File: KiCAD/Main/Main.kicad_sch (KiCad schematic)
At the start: 6 parts, among them J3 Conn_01x02_Socket, J6 Conn_01x02_Socket, J7 Conn_01x02_Socket, J8 Conn_01x02_Socket, U5 LT3092xST, U6 ADG5234BRUZ

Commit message: Add new rf
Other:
- added sheet RF (RF/RF.kicad_sch)
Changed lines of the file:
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@@
+	)
+	(sheet
+		(at 19.05 17.78)
+		(size 27.94 27.94)
+		(exclude_from_sim no)
+		(in_bom yes)
+		(on_board yes)
+		(dnp no)
+		(fields_autoplaced yes)
+		(stroke
+			(width 0.1524)
+			(type solid)
+		)
+		(fill
+			(color 0 0 0 0.0000)
+		)
+		(property "Sheetname" "RF"
+			(at 19.05 17.0684 0)
+			(effects
+				(font
+					(size 1.27 1.27)
+				)
+				(justify left bottom)
+			)
+		)
+		(property "Sheetfile" "RF/RF.kicad_sch"
+			(at 19.05 46.3046 0)
+			(effects
+				(font
+					(size 1.27 1.27)
+				)
+				(justify left top)
+			)
+		)
+		(instances
+			(project "Main"
+				(path "/bbb10697-a5dd-43b8-9c6f-4c5919cf3463"
+					(page "7")
+				)
+			)
+		)
 	)
 	(sheet

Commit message: post meeting update
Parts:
- removed J3, J6, J7, J8: Conn_01x02_Socket, symbol Connector:Conn_01x02_Socket
- removed U5: LT3092xST, Package_TO_SOT_SMD:SOT-223-3_TabPin2, symbol Reference_Current:LT3092xST
- removed U6: ADG5234BRUZ, ADG5234BRUZ:SOP65P640X120-20N, symbol ADG5234BRUZ:ADG5234BRUZ
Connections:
- no-connect marks 4 -> 0
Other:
- sheet GPS & Radio renamed GPS
- added sheet Barometer (Barometric Altimeter/Barometric Altimeter.kicad_sch)
- added sheet Thermistors (Thermistors/Thermistors.kicad_sch)
- sheet GPS ports: added GPS_SCL, GPS_SDA; removed GPS_UART_RX, GPS_UART_TX
- sheet Microcontroller ports: added GPS SCL, GPS SDA, Thermistor_SW1, Thermistor_SW2, Thermistor_SW3, Thermistor_SW4; removed GPS_RX, GPS_TX
- sheet RF ports: added CS_Radio, MISO_Radio, MOSI_Radio, RST_Radio, SCK_Radio; removed none

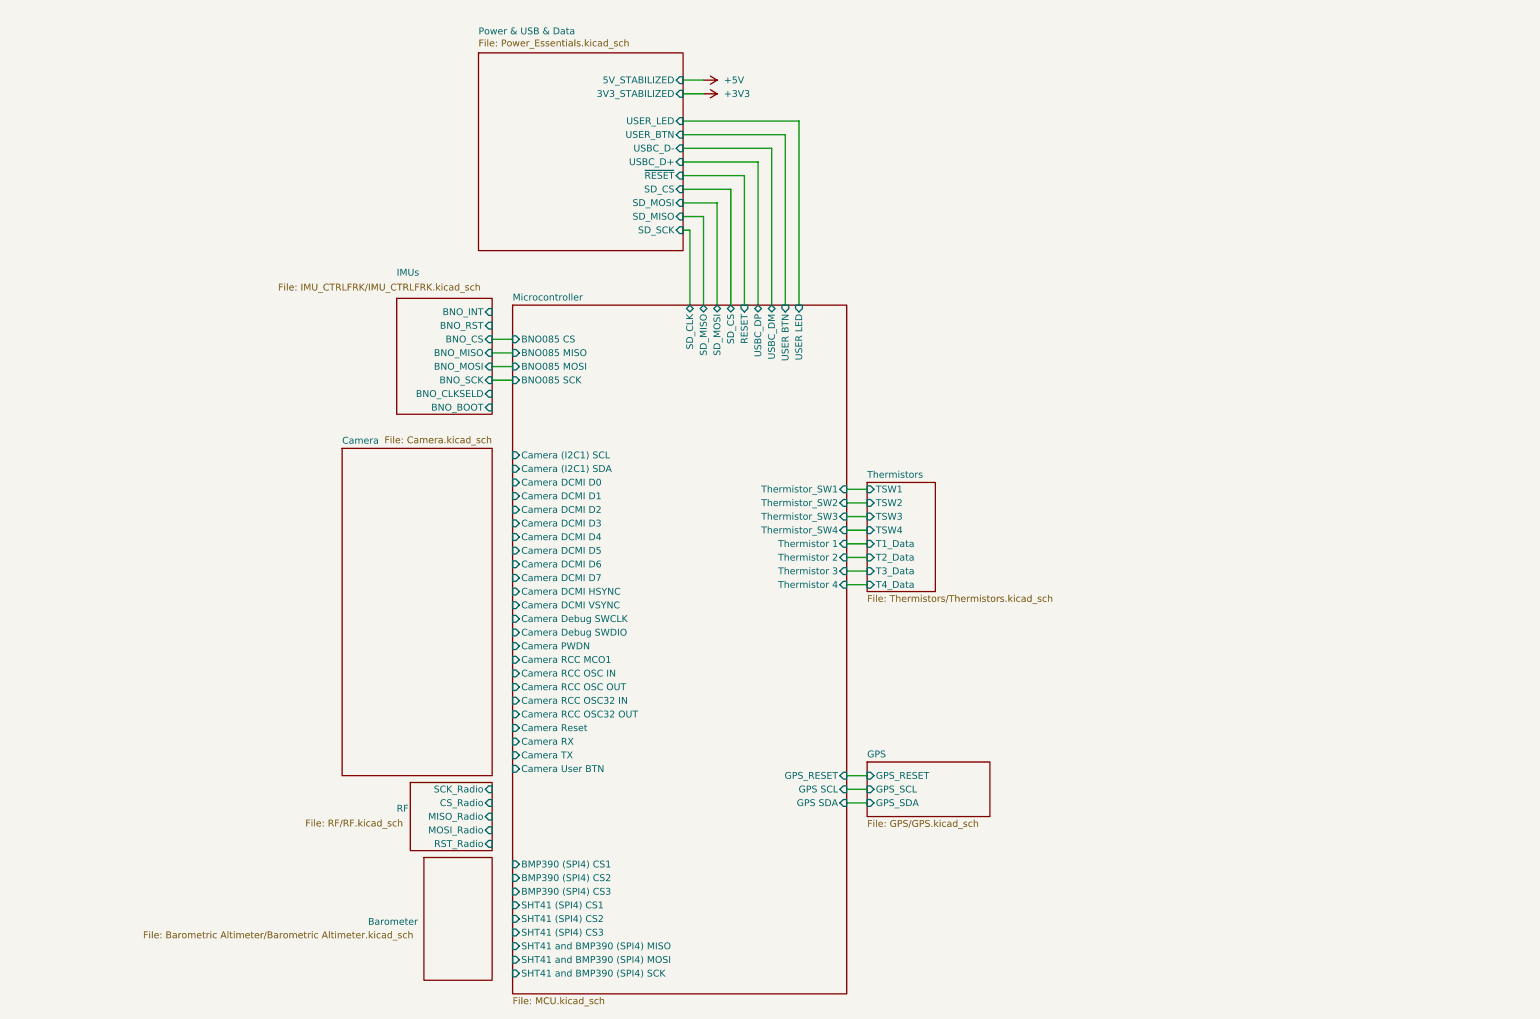
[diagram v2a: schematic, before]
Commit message: Remove thermocouples due to complexity and focus switch
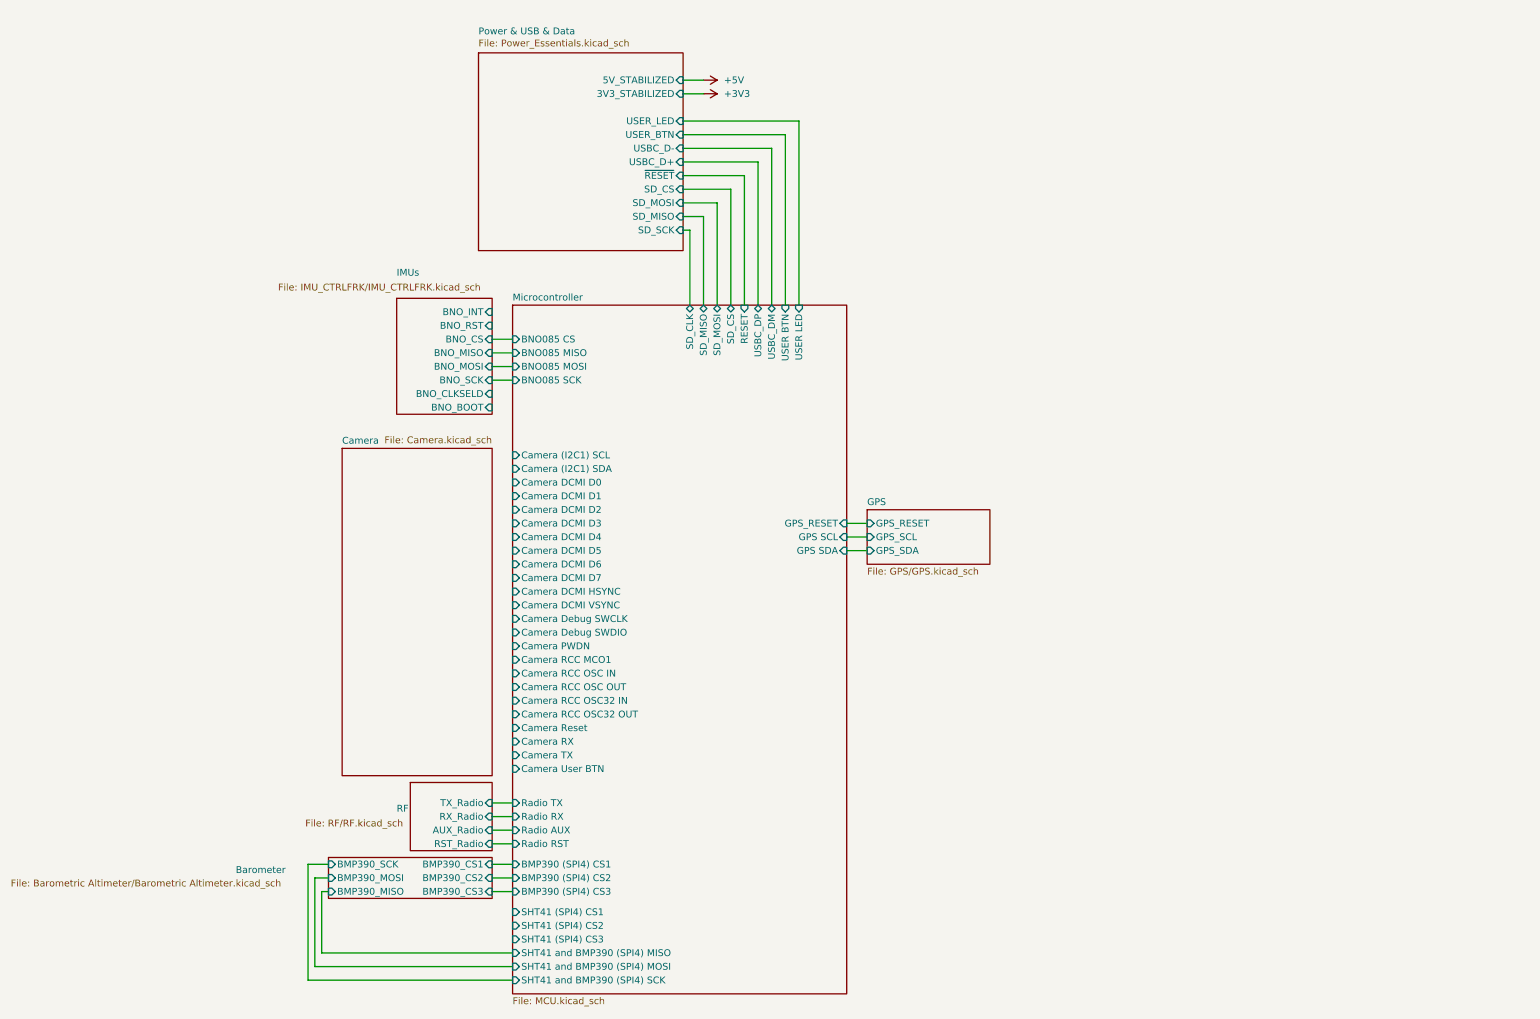
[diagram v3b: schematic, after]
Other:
- removed sheet Thermistors
- sheet Barometer ports: added BMP390_CS1, BMP390_CS2, BMP390_CS3, BMP390_MISO, BMP390_MOSI, BMP390_SCK; removed none
- sheet Microcontroller ports: added Radio AUX, Radio RST, Radio RX, Radio TX; removed Thermistor 1, Thermistor 2, Thermistor 3, Thermistor 4, Thermistor_SW1, Thermistor_SW2, Thermistor_SW3, Thermistor_SW4
- sheet RF ports: added AUX_Radio, RX_Radio, TX_Radio; removed CS_Radio, MISO_Radio, MOSI_Radio, SCK_Radio

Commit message: Keep up to date
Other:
- sheet Microcontroller ports: added Drogue Eject Backup, Drogue Eject Main, Main Eject; removed none
- sheet Power & USB & Data ports: added Drogue Backup Pyro, Drogue Main Pyro, Main Parachute Pyro; removed none
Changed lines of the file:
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@@
 	(wire
 		(pts
-			(xy 138.43 46.99) (xy 144.78 46.99)
+			(xy 138.43 46.99) (xy 147.32 46.99)
 		)
 		(stroke
@@
 	(wire
 		(pts
-			(xy 160.02 31.75) (xy 160.02 66.04)
-		)
-		(stroke
-			(width 0)
-			(type default)
-		)
-	)
-	(wire
-		(pts
-			(xy 138.43 44.45) (xy 147.32 44.45)
-		)
-		(stroke
-			(width 0)
-			(type default)
-		)
-	)
-	(wire
-		(pts
-			(xy 147.32 44.45) (xy 147.32 66.04)
-		)
-		(stroke
-			(width 0)
-			(type default)
-		)
-	)
-	(wire
-		(pts
-			(xy 138.43 52.07) (xy 139.7 52.07)
+			(xy 162.56 31.75) (xy 162.56 66.04)
+		)
+		(stroke
+			(width 0)
+			(type default)
+		)
+	)
+	(wire
+		(pts
+			(xy 124.46 55.88) (xy 124.46 59.69)
+		)
+		(stroke
+			(width 0)
+			(type default)
+		)
+	)
+	(wire
+		(pts
+			(xy 121.92 60.96) (xy 132.08 60.96)
+		)
+		(stroke
+			(width 0)
+			(type default)
+		)
+	)
+	(wire
+		(pts
+			(xy 138.43 44.45) (xy 149.86 44.45)
+		)
+		(stroke
+			(width 0)
+			(type default)
+		)
+	)
+	(wire
+		(pts
+			(xy 149.86 44.45) (xy 149.86 66.04)
+		)
+		(stroke
+			(width 0)
+			(type default)
+		)
+	)
+	(wire
+		(pts
+			(xy 138.43 52.07) (xy 142.24 52.07)
 		)
 		(stroke
@@
 	(wire
 		(pts
-			(xy 138.43 49.53) (xy 142.24 49.53)
+			(xy 138.43 49.53) (xy 144.78 49.53)
 		)
 		(stroke
@@
 	(wire
 		(pts
-			(xy 149.86 41.91) (xy 149.86 66.04)
+			(xy 121.92 55.88) (xy 121.92 60.96)
+		)
+		(stroke
+			(width 0)
+			(type default)
+		)
+	)
+	(wire
+		(pts
+			(xy 152.4 41.91) (xy 152.4 66.04)
 		)
 		(stroke
@@
 	(wire
 		(pts
-			(xy 138.43 41.91) (xy 149.86 41.91)
+			(xy 138.43 41.91) (xy 152.4 41.91)
 		)
 		(stroke
@@
 	(wire
 		(pts
-			(xy 157.48 66.04) (xy 157.48 34.29)
+			(xy 119.38 62.23) (xy 129.54 62.23)
+		)
+		(stroke
+			(width 0)
+			(type default)
+		)
+	)
+	(wire
+		(pts
+			(xy 160.02 66.04) (xy 160.02 34.29)
+		)
+		(stroke
+			(width 0)
+			(type default)
+		)
+	)
+	(wire
+		(pts
+			(xy 124.46 59.69) (xy 134.62 59.69)
 		)
 		(stroke
@@
 	(wire
 		(pts
-			(xy 144.78 46.99) (xy 144.78 66.04)
-		)
-		(stroke
-			(width 0)
-			(type default)
-		)
-	)
-	(wire
-		(pts
-			(xy 138.43 36.83) (xy 154.94 36.83)
+			(xy 147.32 46.99) (xy 147.32 66.04)
+		)
+		(stroke
+			(width 0)
+			(type default)
+		)
+	)
+	(wire
+		(pts
+			(xy 138.43 36.83) (xy 157.48 36.83)
+		)
+		(stroke
+			(width 0)
+			(type default)
+		)
+	)
+	(wire
+		(pts
+			(xy 132.08 60.96) (xy 132.08 66.04)
+		)
+		(stroke
+			(width 0)
+			(type default)
+		)
+	)
+	(wire
+		(pts
+			(xy 134.62 59.69) (xy 134.62 66.04)
 		)
 		(stroke
@@
 	(wire
 		(pts
+			(xy 129.54 62.23) (xy 129.54 66.04)
+		)
+		(stroke
+			(width 0)
+			(type default)
+		)
+	)
+	(wire
+		(pts
 			(xy 71.12 175.26) (xy 71.12 186.69)
 		)
@@
 	(wire
 		(pts
-			(xy 139.7 52.07) (xy 139.7 66.04)
+			(xy 142.24 52.07) (xy 142.24 66.04)
 		)
 		(stroke
@@
 	(wire
 		(pts
-			(xy 138.43 39.37) (xy 152.4 39.37)
-		)
-		(stroke
-			(width 0)
-			(type default)
-		)
-	)
-	(wire
-		(pts
-			(xy 142.24 49.53) (xy 142.24 66.04)
+			(xy 138.43 39.37) (xy 154.94 39.37)
+		)
+		(stroke
+			(width 0)
+			(type default)
+		)
+	)
+	(wire
+		(pts
+			(xy 144.78 49.53) (xy 144.78 66.04)
 		)
 		(stroke
@@
 	(wire
 		(pts
-			(xy 138.43 34.29) (xy 157.48 34.29)
-		)
-		(stroke
-			(width 0)
-			(type default)
-		)
-	)
-	(wire
-		(pts
-			(xy 152.4 66.04) (xy 152.4 39.37)
+			(xy 138.43 34.29) (xy 160.02 34.29)
+		)
+		(stroke
+			(width 0)
+			(type default)
+		)
+	)
+	(wire
+		(pts
+			(xy 154.94 66.04) (xy 154.94 39.37)
 		)
 		(stroke
@@
 	(wire
 		(pts
-			(xy 154.94 36.83) (xy 154.94 66.04)
-		)
-		(stroke
-			(width 0)
-			(type default)
-		)
-	)
-	(wire
-		(pts
-			(xy 138.43 31.75) (xy 160.02 31.75)
+			(xy 157.48 36.83) (xy 157.48 66.04)
+		)
+		(stroke
+			(width 0)
+			(type default)
+		)
+	)
+	(wire
+		(pts
+			(xy 138.43 31.75) (xy 162.56 31.75)
 		)
 		(stroke
@@
 		(pts
 			(xy 106.68 189.23) (xy 69.85 189.23)
+		)
+		(stroke
+			(width 0)
+			(type default)
+		)
+	)
+	(wire
+		(pts
+			(xy 119.38 55.88) (xy 119.38 62.23)
 		)
 		(stroke
@@
 			)
 		)
+		(pin "Drogue Backup Pyro" input
+			(at 124.46 55.88 270)
+			(effects
+				(font
+					(size 1.27 1.27)
+				)
+				(justify left)
+			)
+		)
+		(pin "Drogue Main Pyro" input
+			(at 121.92 55.88 270)
+			(effects
+				(font
+					(size 1.27 1.27)
+				)
+				(justify left)
+			)
+		)
+		(pin "Main Parachute Pyro" input
+			(at 119.38 55.88 270)
+			(effects
+				(font
+					(size 1.27 1.27)
+				)
+				(justify left)
+			)
+		)
 		(instances
 			(project "Main"
@@
 			)
 		)
-		(pin "RESET" input
-			(at 149.86 66.04 90)
-			(effects
-				(font
-					(size 1.27 1.27)
-				)
-				(justify right)
-			)
-		)
 		(pin "SD_CLK" bidirectional
-			(at 139.7 66.04 90)
+			(at 142.24 66.04 90)
 			(effects
 				(font
@@
 		)
 		(pin "SD_MISO" bidirectional
-			(at 142.24 66.04 90)
+			(at 144.78 66.04 90)
 			(effects
 				(font
@@
 		)
 		(pin "SD_MOSI" bidirectional
-			(at 144.78 66.04 90)
+			(at 147.32 66.04 90)
 			(effects
 				(font
@@
 		)
 		(pin "USBC_DM" bidirectional
+			(at 157.48 66.04 90)
+			(effects
+				(font
+					(size 1.27 1.27)
+				)
+				(justify right)
+			)
+		)
+		(pin "USBC_DP" bidirectional
 			(at 154.94 66.04 90)
-			(effects
-				(font
-					(size 1.27 1.27)
-				)
-				(justify right)
-			)
-		)
-		(pin "USBC_DP" bidirectional
-			(at 152.4 66.04 90)
 			(effects
 				(font
@@
 		)
 		(pin "USER BTN" input
-			(at 157.48 66.04 90)
+			(at 160.02 66.04 90)
 			(effects
 				(font
@@
 		)
 		(pin "USER LED" input
-			(at 160.02 66.04 90)
+			(at 162.56 66.04 90)
 			(effects
 				(font
@@
 		)
 		(pin "SD_CS" bidirectional
-			(at 147.32 66.04 90)
+			(at 149.86 66.04 90)
 			(effects
 				(font
@@
 			)
 		)
+		(pin "Drogue Eject Backup" input
+			(at 134.62 66.04 90)
+			(effects
+				(font
+					(size 1.27 1.27)
+				)
+				(justify right)
+			)
+		)
+		(pin "Drogue Eject Main" input
+			(at 132.08 66.04 90)
+			(effects
+				(font
+					(size 1.27 1.27)
+				)
+				(justify right)
+			)
+		)
+		(pin "Main Eject" input
+			(at 129.54 66.04 90)
+			(effects
+				(font
+					(size 1.27 1.27)
+				)
+				(justify right)
+			)
+		)
+		(pin "RESET" input
+			(at 152.4 66.04 90)
+			(effects
+				(font
+					(size 1.27 1.27)
+				)
+				(justify right)
+			)
+		)

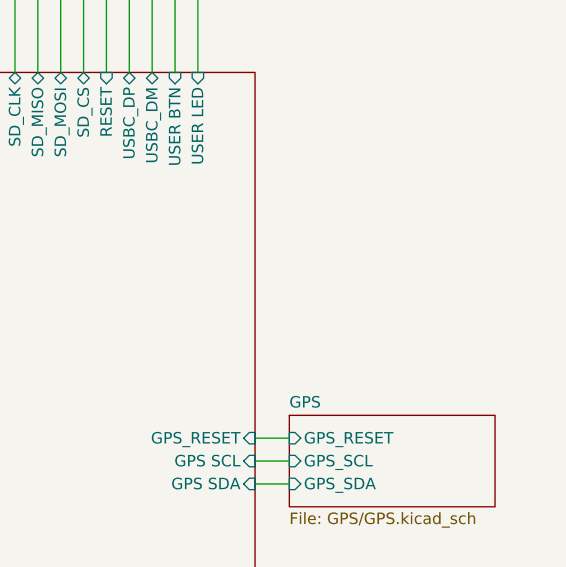
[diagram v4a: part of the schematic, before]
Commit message: Add datasheets and revise TMR goals
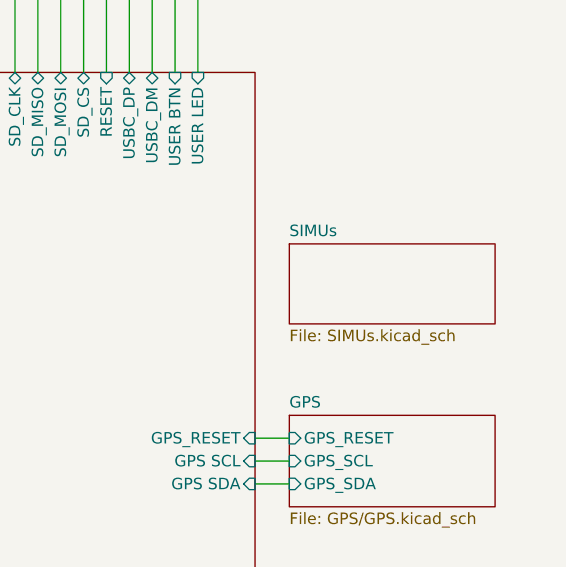
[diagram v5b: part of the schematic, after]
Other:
- added sheet SIMUs (SIMUs.kicad_sch)
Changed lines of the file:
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@@
 			(project "Main"
 				(path "/bbb10697-a5dd-43b8-9c6f-4c5919cf3463"
-					(page "9")
+					(page "8")
 				)
 			)
@@
 				)
 			)
+		)
+	)
+	(sheet
+		(at 172.72 85.09)
+		(size 22.86 8.89)
+		(exclude_from_sim no)
+		(in_bom yes)
+		(on_board yes)
+		(dnp no)
+		(fields_autoplaced yes)
+		(stroke
+			(width 0.1524)
+			(type solid)
+		)
+		(fill
+			(color 0 0 0 0.0000)
+		)
+		(property "Sheetname" "SIMUs"
+			(at 172.72 84.3784 0)
+			(effects
+				(font
+					(size 1.27 1.27)
+				)
+				(justify left bottom)
+			)
+		)
+		(property "Sheetfile" "SIMUs.kicad_sch"
+			(at 172.72 94.5646 0)
+			(effects
+				(font
+					(size 1.27 1.27)
+				)
+				(justify left top)
+			)
+		)
+		(instances
+			(project "Main"
+				(path "/bbb10697-a5dd-43b8-9c6f-4c5919cf3463"
+					(page "9")
+				)
+			)

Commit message: Polish for review
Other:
- removed sheet Camera
- added sheet SHT41 (SHT41.kicad_sch)
- sheet Barometer ports: added BMP390 INT1, BMP390 INT2, BMP390 INT3; removed none
- sheet Microcontroller ports: added BMP390 (SPI4) MISO, BMP390 (SPI4) MOSI, BMP390 (SPI4) SCK, BMP390 INT1, BMP390 INT2, BMP390 INT3, BNO085 INT, BNO085 RST, SD CS, SD MOSI, SHT41 SCL, SHT41 SDA, SIMU CLK, SIMU CS1, SIMU CS2, SIMU CS3, SIMU MISO, SIMU MOSI, SIMU1 INT, SIMU2 INT, SIMU3 INT; removed Camera (I2C1) SCL, Camera (I2C1) SDA, Camera DCMI D0, Camera DCMI D1, Camera DCMI D2, Camera DCMI D3, Camera DCMI D4, Camera DCMI D5, Camera DCMI D6, Camera DCMI D7, Camera DCMI HSYNC, Camera DCMI VSYNC, Camera Debug SWCLK, Camera Debug SWDIO, Camera PWDN, Camera RCC MCO1, Camera RCC OSC IN, Camera RCC OSC OUT, Camera RCC OSC32 IN, Camera RCC OSC32 OUT, Camera RX, Camera Reset, Camera TX, Camera User BTN, SD_CS, SD_MOSI, SHT41 (SPI4) CS1, SHT41 (SPI4) CS2, SHT41 (SPI4) CS3, SHT41 and BMP390 (SPI4) MISO, SHT41 and BMP390 (SPI4) MOSI, SHT41 and BMP390 (SPI4) SCK
- sheet SIMUs ports: added SIMU CLK, SIMU CS1, SIMU CS2, SIMU CS3, SIMU MISO, SIMU MOSI, SIMU1 INT1, SIMU2 INT1, SIMU3 INT1; removed none
